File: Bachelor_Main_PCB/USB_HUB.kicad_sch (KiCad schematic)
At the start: 17 parts, among them J29 M20-9990245, U11 USB2514B-I/M2

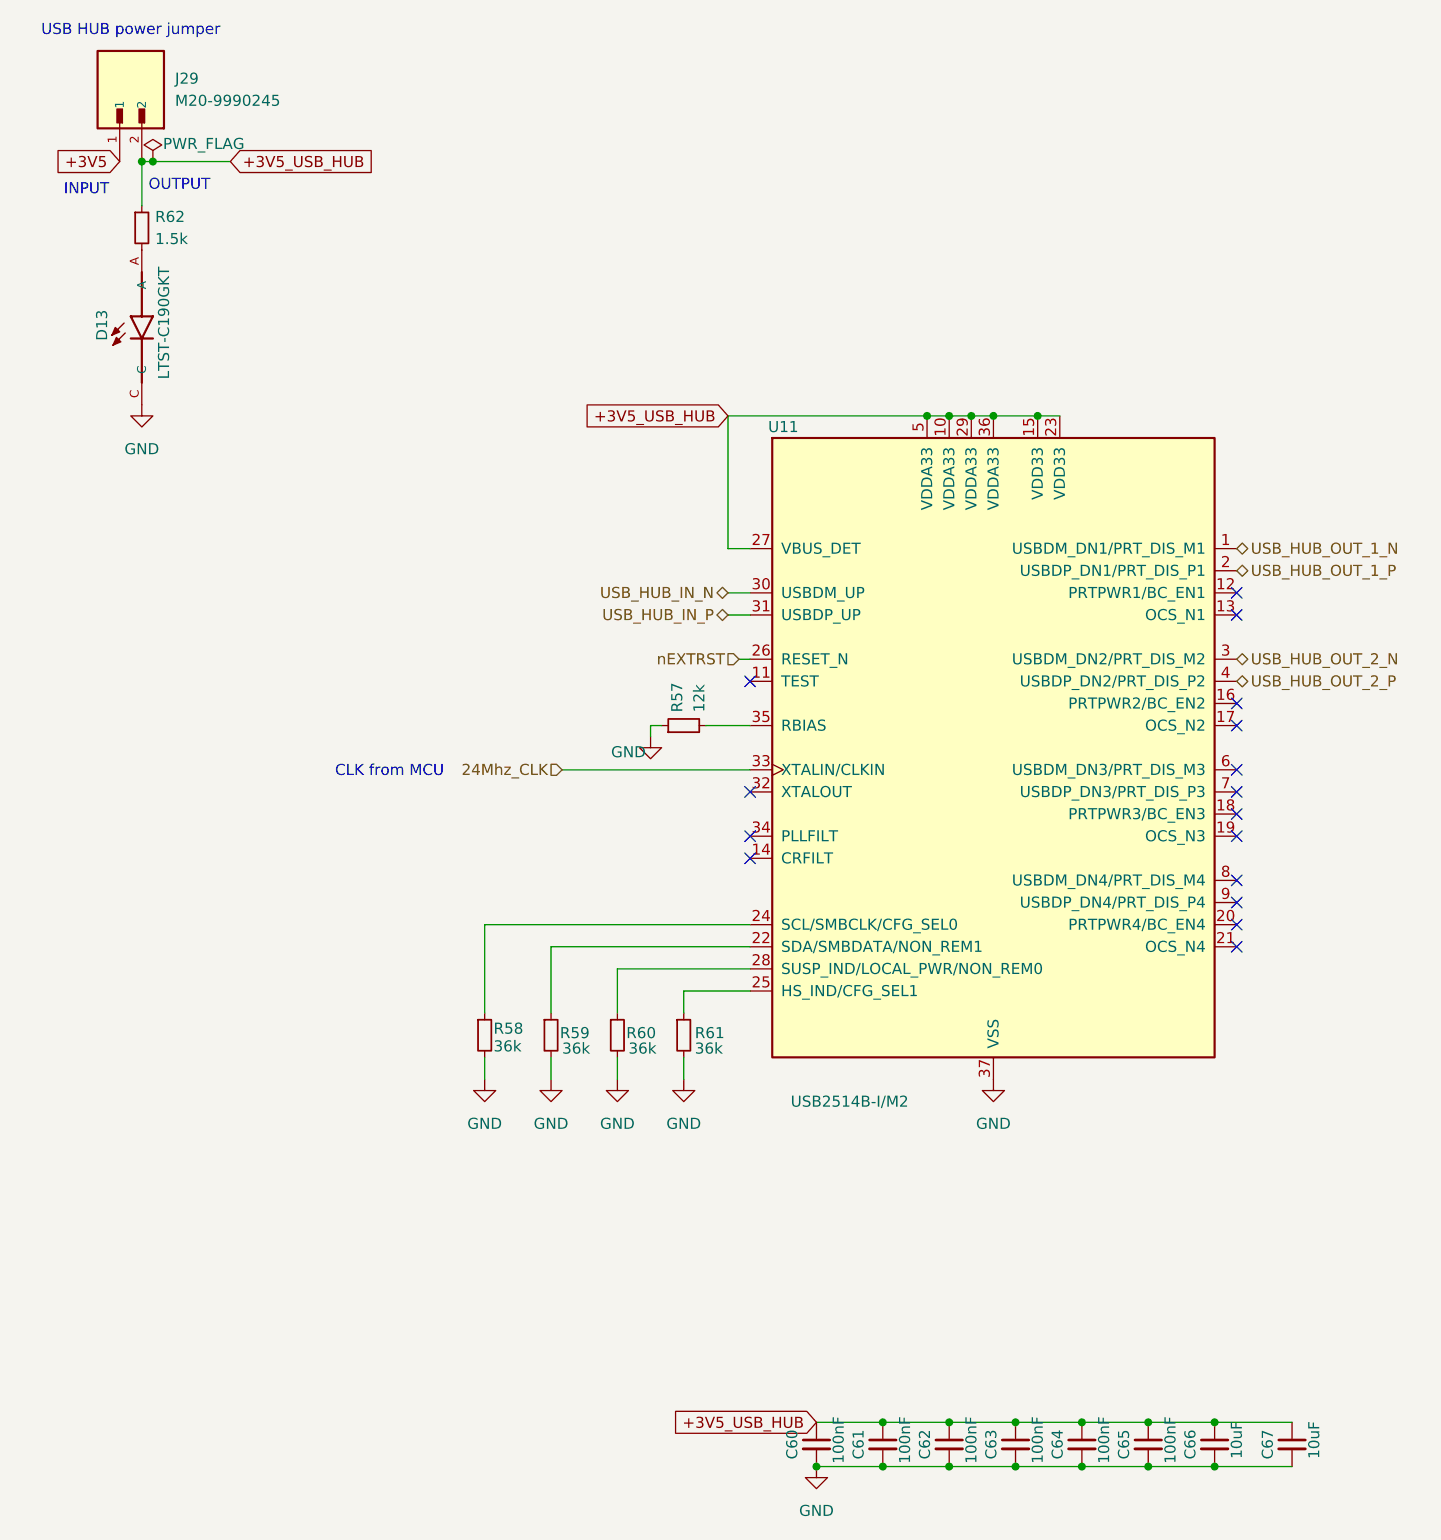
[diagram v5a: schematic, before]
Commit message: Add MPN to all resistors. Only missing pinheaders
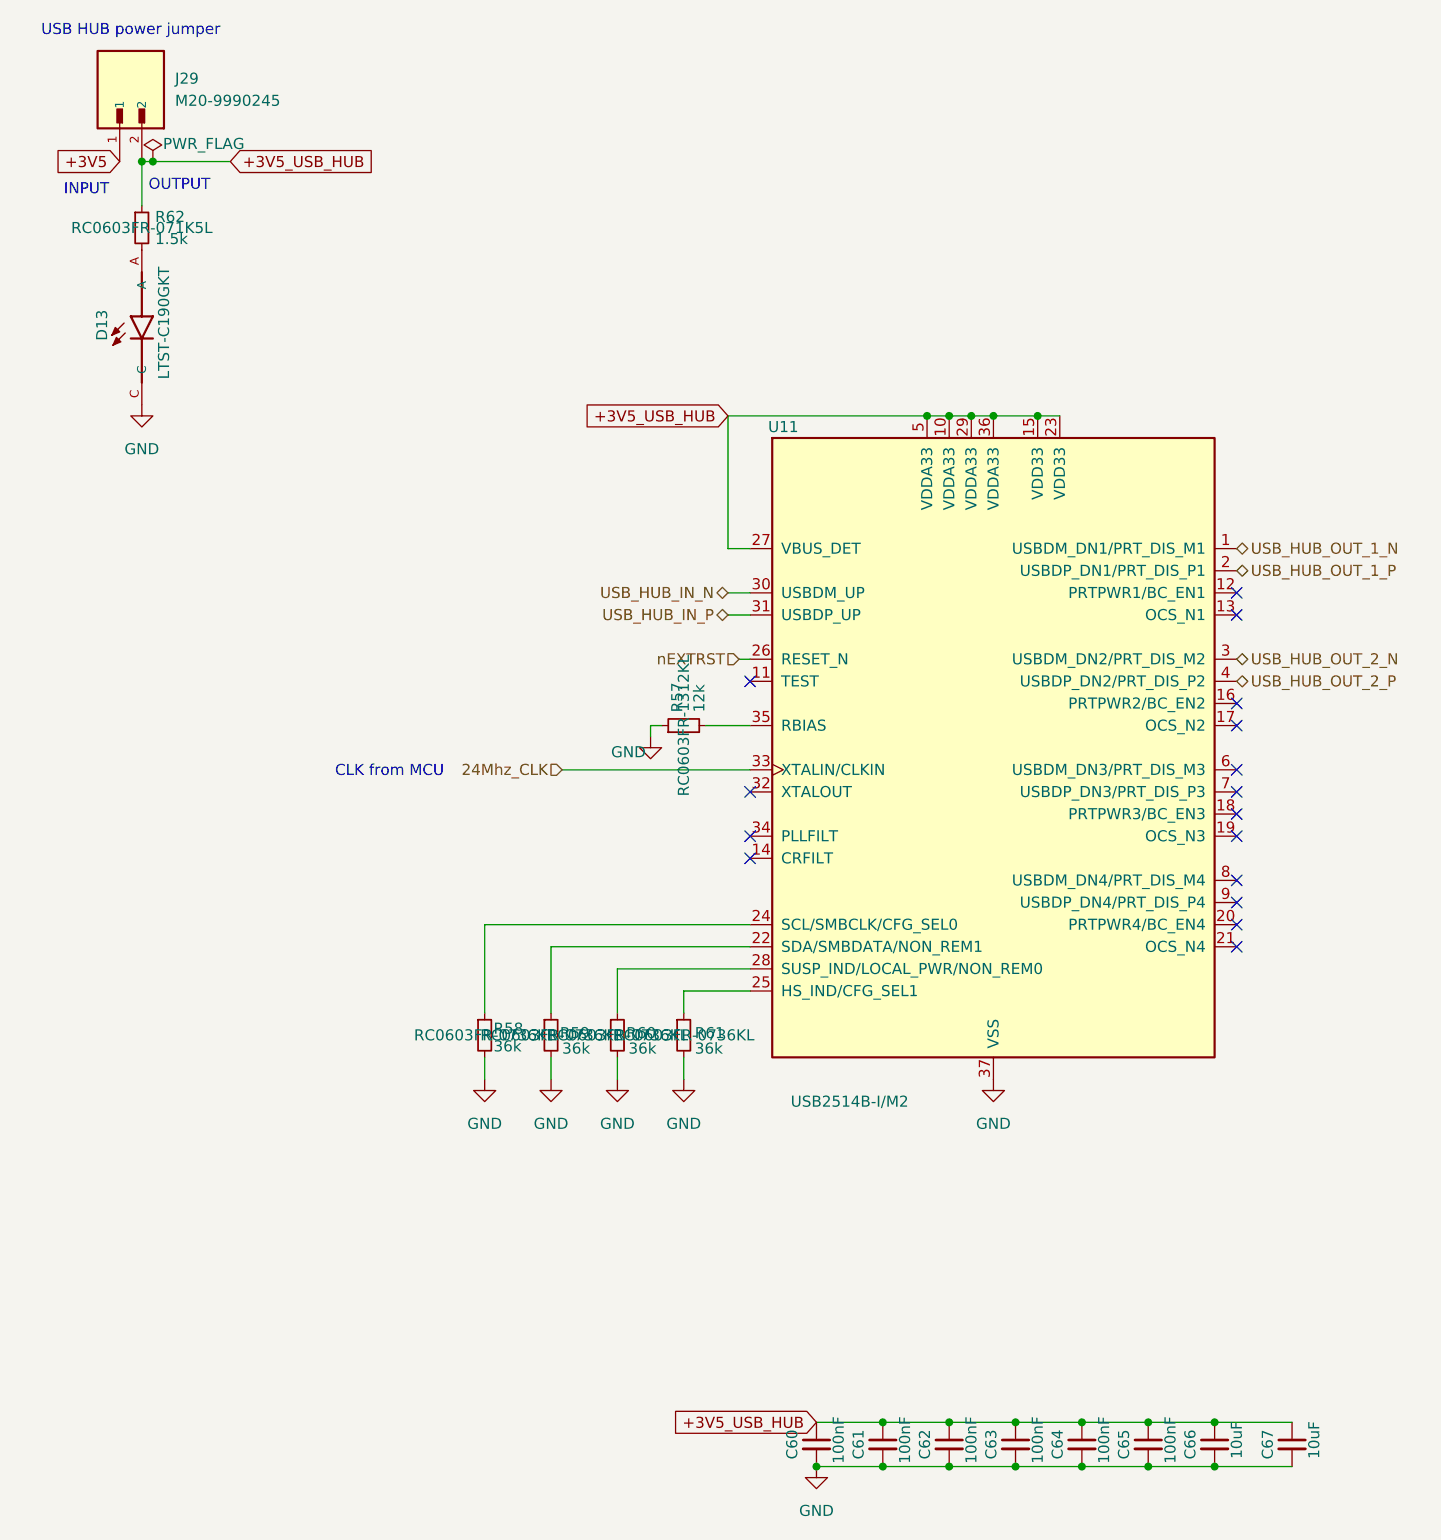
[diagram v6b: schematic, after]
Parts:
- R57: Part-no (none) -> RC0603FR-1312KL
- R58, R59, R60, R61: Part-no (none) -> RC0603FR-0736KL
- R62: Part-no (none) -> RC0603FR-071K5L
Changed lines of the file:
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@@
+			)
+		)
+		(property "Part-no" "RC0603FR-0736KL"
+			(at 72.39 133.35 0)
+			(effects
+				(font
+					(size 1.27 1.27)
+				)
 			)
 		)
@@
 			)
 		)
+		(property "Part-no" "RC0603FR-071K5L"
+			(at 33.02 40.64 0)
+			(effects
+				(font
+					(size 1.27 1.27)
+				)
+			)
+		)
 		(pin "1"
 		)
@@
 				)
 				(hide yes)
+			)
+		)
+		(property "Part-no" "RC0603FR-1312KL"
+			(at 95.25 97.79 0)
+			(effects
+				(font
+					(size 1.27 1.27)
+				)
 			)
 		)
@@
 			)
 		)
+		(property "Part-no" "RC0603FR-0736KL"
+			(at 80.01 133.35 0)
+			(effects
+				(font
+					(size 1.27 1.27)
+				)
+			)
+		)
 		(pin "1"
 		)
@@
 			)
 		)
+		(property "Part-no" "RC0603FR-0736KL"
+			(at 87.63 133.35 0)
+			(effects
+				(font
+					(size 1.27 1.27)
+				)
+			)
+		)
 		(pin "1"
 		)
@@
 			)
 		)
+		(property "Part-no" "RC0603FR-0736KL"
+			(at 95.25 133.35 0)
+			(effects
+				(font
+					(size 1.27 1.27)
+				)
+			)
+		)
